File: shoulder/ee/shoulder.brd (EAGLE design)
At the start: 45.7 x 68.6 mm, 34 parts, among them IC3 XMEGA-A4, J1(RS) RJ11-6PTH, J2(LS) RJ11-6PTH, T1 2N2222

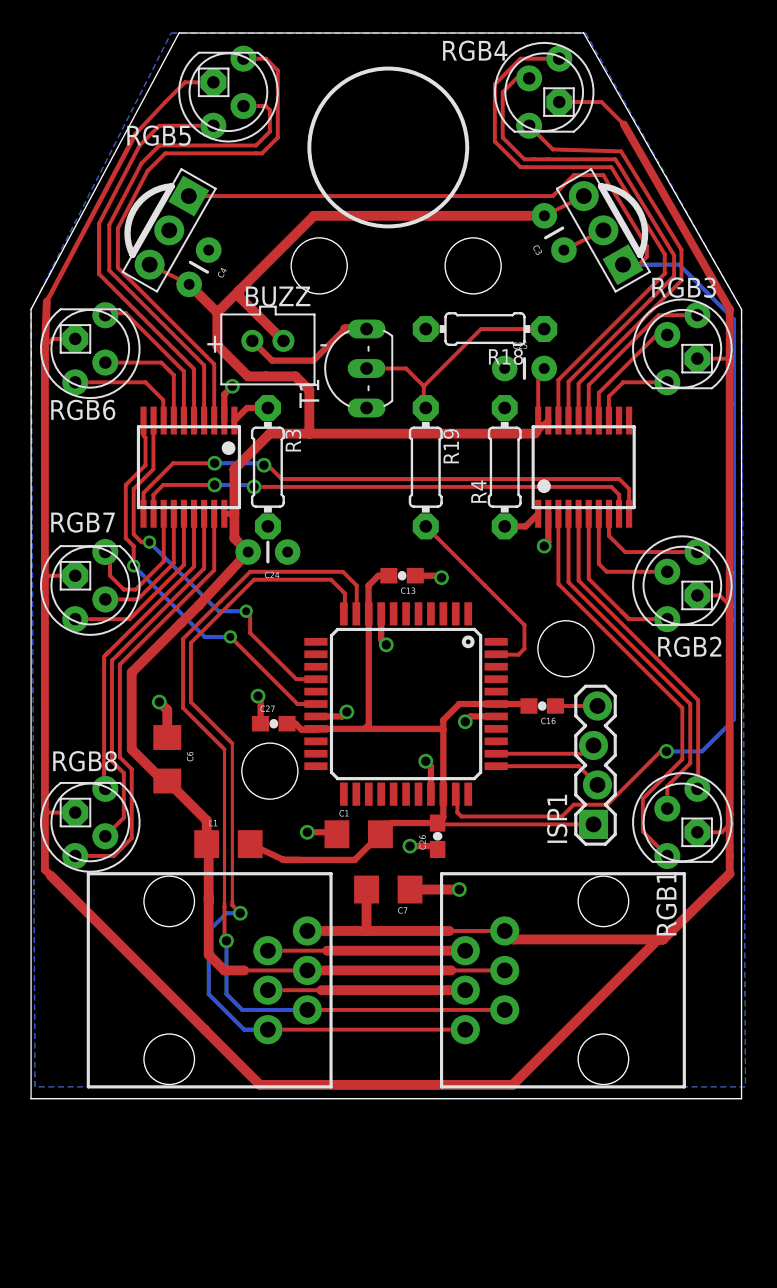
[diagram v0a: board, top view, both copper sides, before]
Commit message: shoulder: schematic updates for new board
- all through hole resistors replaced with 0603
- All through hole capacitors replaced with 0603
- through hole LEDs replaced with SMT
- Added jumpers to switch between SPI and USART peripheral for LED
  controllers
    - USART in SPI master mode allows DMA.
- Added reset button.
- Added a pullup on AVR reset line.
- Moved T1 and BUZZ (JST conn) further from screw holes.
- Moved vibrator further from screw holes.
- Replaced IR receivers with SMT heimdall package
- Added a footprint for a 3rd IR receiver (facing up)
- Replaced through hole NPN transistor with SMT
- Replaced 4 pin ISP with 6 pin 50mil RA header.
- Added frame to schematic :o
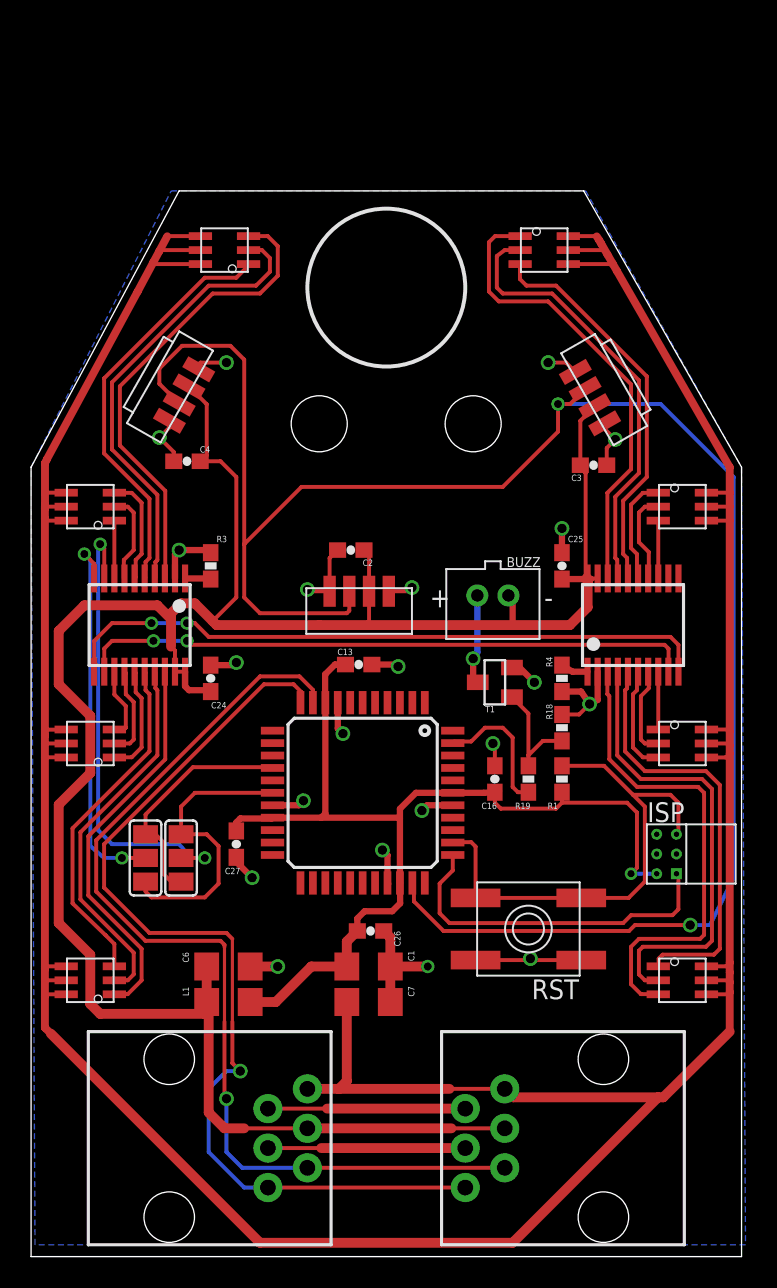
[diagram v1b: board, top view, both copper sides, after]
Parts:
- removed ISP1: (no value), SparkFun-Connectors:1X04_LOCK
- added C2: 0.1uF, SparkFun-Capacitors:0603-CAP
- added ISP: PDI, greg:IDC-2X10-50MIL-UNSHROUDED
- added R1: (no value), SparkFun-Resistors:0603-RES
- added RST: SPST_TACT-EVQQ2, adafruit:EVQ-Q2
- added SJ1, SJ2: (no value), SparkFun-Passives:SJ_2
- added U$3: TSMP77000UP, greg:HEIMDALL-UP
- C24, C25, C3, C4: device SparkFun-Passives:CAP-PTH-SMALL -> SparkFun-Capacitors:0603-CAP
- R18, R19, R3, R4: device adafruit:0204/7 -> SparkFun-Resistors:0603-RES
- RGB1, RGB2, RGB3, RGB4, RGB5, RGB6, RGB7, RGB8: value RGBLED_CA-5MM -> AVAGO-RGB-SMT; device adafruit:LED5MMRGB -> greg:AVAGO-SMT-RGB
- T1: value 2N2222 -> (none); device adafruit:TO92-EBC-OVAL -> SparkFun-DiscreteSemi:SOT23
- U$1, U$2: value PNA460XM -> TSMP77000SIDE; device adafruit:PNA460XM -> greg:TSMP77000
- moved R18 26.1 mm to (34.2, 34.0), turned to 90 degrees
- moved T1 22.3 mm to (29.8, 37.0)
- moved BUZZ 21.9 mm to (29.7, 42.5)
- moved R19 21.1 mm to (32.0, 30.7)
- moved R4 14.1 mm to (34.2, 37.2), turned to 90 degrees
- moved C3 14.0 mm to (36.2, 50.9), turned to 180 degrees
- moved C6 13.9 mm to (12.7, 18.7), turned to 180 degrees
- moved C4 13.7 mm to (10.0, 51.2), turned to 0 degrees
- moved C25 13.2 mm to (34.2, 44.5), turned to 270 degrees
- moved U$1 11.3 mm to (10.7, 54.9), turned to 60.3 degrees
- moved U$2 11.3 mm to (35.1, 54.9), turned to 299.7 degrees
- moved LC1 10.6 mm to (38.7, 40.6)
- moved LC2 10.6 mm to (6.99, 40.6)
- moved RGB5 10.2 mm to (12.4, 64.8), turned to 90 degrees
- moved RGB4 10.2 mm to (33.0, 64.8), turned to 270 degrees
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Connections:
- removed net N$4: IC3.15, LC2.9
- removed net N$7: IC3.35, ISP1.3
- new net LED-SCK: LC2.10, SJ1.2
- new net LED-SCK/TXD: IC3.17, SJ1.3, SJ2.3
- new net LED-SDI: LC2.9, SJ2.2
- new net LED-XCK/SDO: IC3.15, SJ1.1, SJ2.1
- net +3V3: now also C2.2, U$1.P$2, U$2.P$2, U$3.P$2; no longer U$1.3, U$2.3
- net +7V2: now also RGB1.P$4, RGB1.P$5, RGB1.P$6, RGB2.P$4, RGB2.P$5, RGB2.P$6, RGB3.P$4, RGB3.P$5, RGB3.P$6, RGB4.P$4, RGB4.P$5, RGB4.P$6, RGB5.P$4, RGB5.P$5, RGB5.P$6, RGB6.P$4, RGB6.P$5, RGB6.P$6, RGB7.P$4, RGB7.P$5, RGB7.P$6, RGB8.P$4, RGB8.P$5, RGB8.P$6; no longer RGB1.2, RGB2.2, RGB3.2, RGB4.2, RGB5.2, RGB6.2, RGB7.2, RGB8.2
- net GND: now also C2.1, ISP.6, RST.A, RST.A', T1.2, U$1.P$1, U$1.P$4, U$2.P$1, U$2.P$4, U$3.P$1, U$3.P$4; no longer ISP1.4, T1.E, U$1.2, U$2.2
- net IRX-SH: now also U$1.P$3, U$2.P$3, U$3.P$3; no longer U$1.1, U$2.1
- net N$10: now also RGB5.P$3; no longer RGB5.1
- net N$11: now also RGB6.P$3; no longer RGB6.1
- net N$14: now also T1.3; no longer T1.C
- net N$17: now also RGB3.P$1; no longer RGB3.4
- net N$19: now also T1.1; no longer T1.B
- net N$24: now also RGB3.P$3; no longer RGB3.1
- net N$27: now also RGB3.P$2; no longer RGB3.3
- net N$31: now also RGB4.P$3; no longer RGB4.1
- net N$32: now also RGB4.P$2; no longer RGB4.3
- net N$33: now also RGB4.P$1; no longer RGB4.4
- net N$36: now also RGB1.P$2; no longer RGB1.3
- net N$37: now also RGB1.P$1; no longer RGB1.4
- net N$38: now also RGB2.P$3; no longer RGB2.1
- net N$39: now also RGB2.P$2; no longer RGB2.3
- net N$40: now also RGB2.P$1; no longer RGB2.4
- net N$42: now also RGB5.P$2; no longer RGB5.3
- net N$43: now also RGB5.P$1; no longer RGB5.4
- net N$49: now also RGB6.P$2; no longer RGB6.3
- net N$5: now also IC3.35, ISP.5, R1.1, RST.B, RST.B'; no longer IC3.17, LC2.10
- net N$50: now also RGB6.P$1; no longer RGB6.4
- net N$51: now also RGB8.P$3; no longer RGB8.1
- net N$52: now also RGB8.P$2; no longer RGB8.3
- net N$53: now also RGB8.P$1; no longer RGB8.4
- net N$54: now also RGB7.P$1; no longer RGB7.4
- net N$55: now also RGB7.P$2; no longer RGB7.3
- net N$56: now also RGB7.P$3; no longer RGB7.1
- net N$6: now also ISP.1; no longer ISP1.2
- net N$8: now also RGB1.P$3; no longer RGB1.1
- net N$9: now also ISP.2, R1.2; no longer ISP1.1
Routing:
- net IRX-SH: track 91.1 -> 123.8 mm, vias 1 -> 2
- net GND: track 57.3 -> 88.1 mm, vias 12 -> 21
- net LED-SDI: track 0.00 -> 29.9 mm, vias 0 -> 2
- net +7V2: track 205.1 -> 234.6 mm
- net LED-SCK: track 0.00 -> 24.6 mm, vias 0 -> 2
- net N$4: track 24.1 -> 0.00 mm, vias 2 -> 0
- net LED-SCK/TXD: track 0.00 -> 18.4 mm
- net +3V3: track 132.4 -> 149.2 mm
- net LED-XCK/SDO: track 0.00 -> 15.5 mm
- net N$6: track 7.02 -> 22.4 mm
- net N$9: track 58.4 -> 66.2 mm, vias 0 -> 1
- net N$19: track 14.9 -> 7.41 mm
- net N$36: track 22.8 -> 30.1 mm
- net N$5: track 25.5 -> 32.7 mm, vias 2 -> 0
- net LIGHTS-SCL: track 56.0 -> 63.0 mm
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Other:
- board text added: "*"
- board text added: "BOWSER"
- board text added: "SPI"
- board text added: "USART"
- board text added: "rev 2"
- board text removed: "G4 shoulder r1"

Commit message: Moved filter caps and added test points
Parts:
- added 3V3, GND, TP1, TP5, TP6, VSYS: PTR1PAD1-17, testpad:P1-17
- R1: value (none) -> 10k
- R3, R4: value (none) -> 2k4
- moved R1 2.62 mm to (31.9, 29.5)
- moved R19 2.04 mm to (31.9, 32.8), turned to 270 degrees
- moved C13 1.78 mm to (19.3, 38.2)
- moved C26 1.59 mm to (23.2, 21.7), turned to 0 degrees
- moved C27 1.40 mm to (13.2, 27.9), turned to 270 degrees
- moved C16 1.30 mm to (29.6, 29.5), turned to 90 degrees
- moved R18 1.27 mm to (34.2, 32.8)
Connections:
- net +3V3: now also 3V3.TP
- net +7V2: now also VSYS.TP
- net GND: now also GND.TP
- net IRX-SH: now also TP1.TP
- net LED-SCK: now also TP5.TP
- net LED-SDI: now also TP6.TP
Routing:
- net +3V3: track 149.2 -> 163.9 mm
- net LED-SCK: track 24.6 -> 37.2 mm
- net IRX-SH: track 123.8 -> 130.8 mm
- net LED-SCK/TXD: track 18.4 -> 23.1 mm
- net LED-SDI: track 29.9 -> 34.0 mm, vias 2 -> 1
- net VIBRATOR: track 8.89 -> 5.05 mm
- net GND: track 88.1 -> 90.8 mm, vias 21 -> 19
- net +7V2: track 234.6 -> 236.9 mm
- net N$5: track 32.7 -> 34.5 mm
- net N$9: track 66.2 -> 65.3 mm
- net N$19: track 7.41 -> 8.04 mm
- net LIGHTS-SCL: track 63.0 -> 63.7 mm

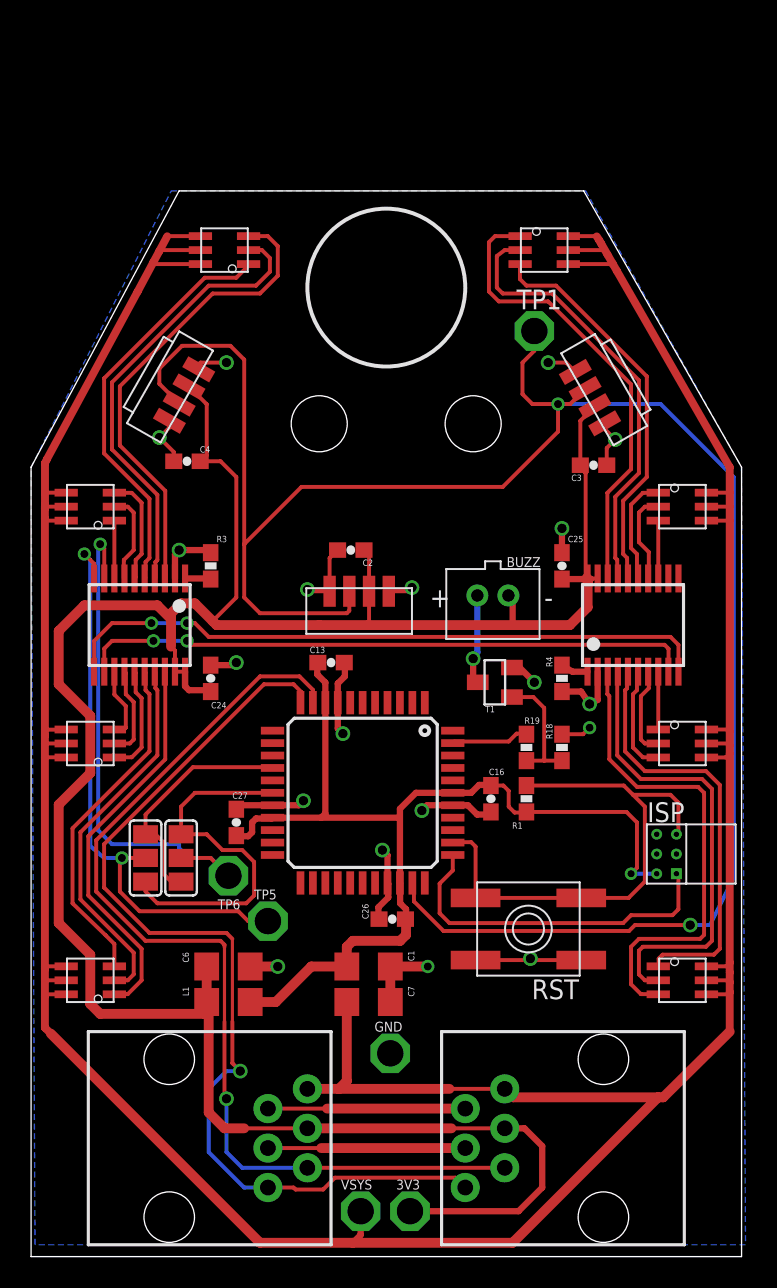
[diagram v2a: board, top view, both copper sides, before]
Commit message: shoulder board: fix rev2 bugs
- Bump board revision to rev3
- Remove USART/SPI jumper - USART works fine
    - resolves GF-38
- Fix ISP pin hole sizing
    - resolves GF-37
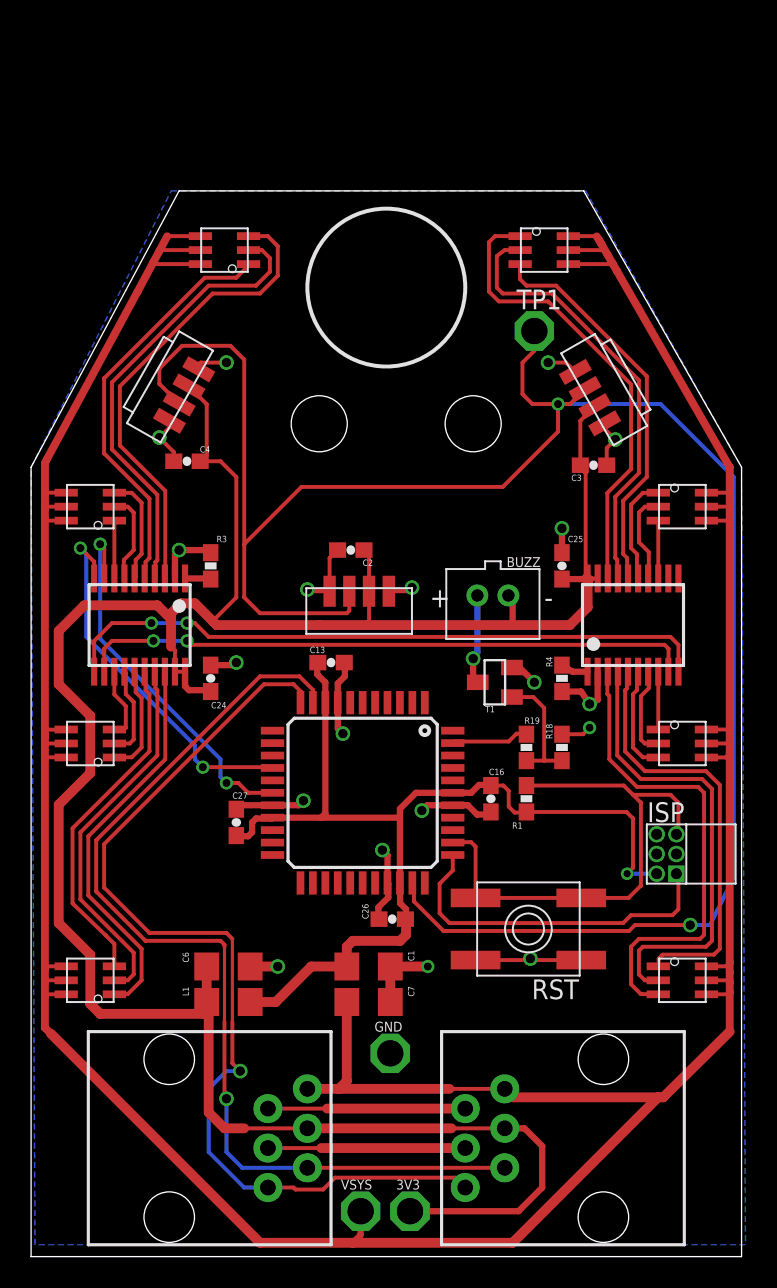
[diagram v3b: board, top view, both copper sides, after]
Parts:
- removed SJ1, SJ2: (no value), SparkFun-Passives:SJ_2
- removed TP5, TP6: PTR1PAD1-17, testpad:P1-17
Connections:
- removed net LED-SCK: LC2.10, SJ1.2, TP5.TP
- removed net LED-SDI: LC2.9, SJ2.2, TP6.TP
- net LED-SCK/TXD: now also LC2.9; no longer SJ1.3, SJ2.3
- net LED-XCK/SDO: now also LC2.10; no longer SJ1.1, SJ2.1
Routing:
- net LED-SCK: track 37.2 -> 0.00 mm, vias 2 -> 0
- net LED-SDI: track 34.0 -> 0.00 mm, vias 1 -> 0
- net LED-XCK/SDO: track 15.5 -> 24.2 mm, vias 0 -> 2
- net LED-SCK/TXD: track 23.1 -> 24.3 mm, vias 0 -> 2
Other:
- board text added: "rev 3"
- board text removed: "SPI"
- board text removed: "USART"
- board text removed: "rev 2"

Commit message: Shoulder rev4 hardware
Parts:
- removed C13, C16, C26, C27: 100nF, SparkFun-Passives:0603-CAP
- removed IC3: XMEGA-A4, xmega:TQFP44
- removed ISP: PDI, greg:IDC-2X10-50MIL-UNSHROUDED
- added C10, C11, C12, C9: 100nF, SparkFun-Passives:0603-CAP
- added C5: 10uF, SparkFun-Passives:0603-CAP
- added C8: 1uF, SparkFun-Passives:0603-CAP
- added JP1: CORTEX_DEBUGPTH, greg:2X5-PTH-1.27MM
- added L2: (no value), SparkFun-Passives:0603
- added L3: 10uH, SparkFun-Passives:0805
- added R2: 1k, SparkFun-Resistors:0603-RES
- added R5: 330, SparkFun-Resistors:0603-RES
- added U1: ATSAML21E-A, greg:TQFP-32-7X7-0.8MM
- C1: device SparkFun-Passives:1206 -> SparkFun-Passives:0603-CAP
- L1: value (none) -> 10uH; device greg:1206 -> SparkFun-Passives:0805
- moved L1 21.5 mm to (19.3, 36.8), turned to 270 degrees
- moved C1 8.90 mm to (12.8, 19.2), turned to 90 degrees
- moved RST 4.27 mm to (34.5, 24.5)
- moved C6 4.12 mm to (16.1, 16.4)
- turned C7 to 0 degrees
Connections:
- removed net N$9: C1.2, C13.2, C16.2, C26.2, C27.2, IC3.19, IC3.31, IC3.39, IC3.9, ISP.2, L1.2, R1.2
- new net N$12: C8.1, C9.1, L1.1, U1.27
- new net N$4: C10.2, C5.2, L2.1, U1.9
- new net N$7: L1.2, U1.29
- new net RST: C12.2, JP1.10, R1.1, R5.1, U1.26
- new net SWCLK: JP1.4, R2.2, U1.31
- new net SWDIO: JP1.2, U1.32
- net +3V3: now also JP1.1, L3.1, R1.2, R2.1; no longer L1.1
- net GND: now also C10.1, C11.1, C12.1, C5.1, C8.2, C9.2, JP1.3, JP1.5, U1.10, U1.28; no longer C13.1, C16.1, C26.1, C27.1, IC3.18, IC3.30, IC3.38, IC3.8, ISP.6
- net IRX-SH: now also U1.11; no longer IC3.32
- net LED-SCK/TXD: now also U1.5; no longer IC3.17
- net LED-XCK/SDO: now also U1.6; no longer IC3.15
- net LIGHTS-SCL: now also U1.18, U1.22; no longer IC3.11
- net LIGHTS-SDA: now also U1.17, U1.21; no longer IC3.10
- net N$5: now also C1.2, C11.2, L2.2, L3.2, U1.30; no longer IC3.35, ISP.5, R1.1, RST.B, RST.B'
- net N$6: now also R5.2, RST.B, RST.B'; no longer IC3.34, ISP.1
- net VIBRATOR: now also U1.25; no longer IC3.43
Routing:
- net N$9: track 65.4 -> 0.00 mm, vias 1 -> 0
- net +3V3: track 163.9 -> 206.3 mm, vias 0 -> 2
- net RST: track 0.00 -> 33.7 mm
- net SWCLK: track 0.00 -> 24.7 mm, vias 0 -> 1
- net LIGHTS-SDA: track 64.2 -> 42.8 mm
- net SWDIO: track 0.00 -> 16.9 mm
- net LIGHTS-SCL: track 63.7 -> 48.8 mm
- net N$6: track 22.4 -> 8.96 mm
- net N$12: track 0.00 -> 10.0 mm
- net N$5: track 34.2 -> 25.2 mm, vias 0 -> 2
- net N$4: track 0.00 -> 6.51 mm
- net IRX-SH: track 130.8 -> 135.5 mm, vias 2 -> 4
- net GND: track 90.8 -> 87.3 mm, vias 19 -> 20
- net VIBRATOR: track 5.05 -> 8.11 mm
- net N$7: track 0.00 -> 3.04 mm
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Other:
- board text added: "rev 4"
- board text removed: "rev 3"
